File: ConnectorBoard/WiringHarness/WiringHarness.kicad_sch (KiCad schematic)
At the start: 9 parts, among them J1 Barrel_Jack, J2 Conn_01x03, J3 Conn_01x03, J4 Conn_01x04, U1 L7805, U2 L7805

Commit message: Wiring harness probably OK
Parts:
- removed J4: Conn_01x04, symbol Connector_Generic:Conn_01x04
- added C3, C4: 1uF, Capacitor_SMD:C_0603_1608Metric, symbol Device:C_Small
- added H1, H2, H3, H4: MountingHole, MountingHole:MountingHole_2.2mm_M2, symbol Mechanical:MountingHole
- added J4: Conn_02x05_Odd_Even, Connector_PinHeader_2.54mm:PinHeader_2x05_P2.54mm_Vertical, symbol Connector_Generic:Conn_02x05_Odd_Even
- C1, C2: footprint Capacitor_SMD:C_0805_2012Metric -> Capacitor_SMD:C_0603_1608Metric
- FB1: footprint (none) -> Inductor_SMD:L_0603_1608Metric
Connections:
- net Visol: now reaches C2.1, FB1.2, U2.1 (IN)
- net GND: now reaches C1.2, C2.2, J1.2, J2.3 (Pin_3), J3.3 (Pin_3), U1.2 (GND), U2.2 (GND)
- net GND: now also C3.2, C4.2, J4.2 (Pin_2)
- net Vsys: now reaches U2.3 (OUT)
- net Vsys: now also C3.1, J4.4 (Pin_4)
- net ServoY: now reaches J2.1 (Pin_1)
- net ServoY: now also J4.8 (Pin_8)
- net VoutServo: now reaches J2.2 (Pin_2), J3.2 (Pin_2), U1.3 (OUT)
- net VoutServo: now also C4.1
- net ServoX: now reaches J3.1 (Pin_1)
- net ServoX: now also J4.6 (Pin_6)
- net +12V: now reaches C1.1, FB1.1, J1.1, U1.1 (IN)
- no-connect marks 0 -> 6
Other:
- moved on the sheet: J2, J3

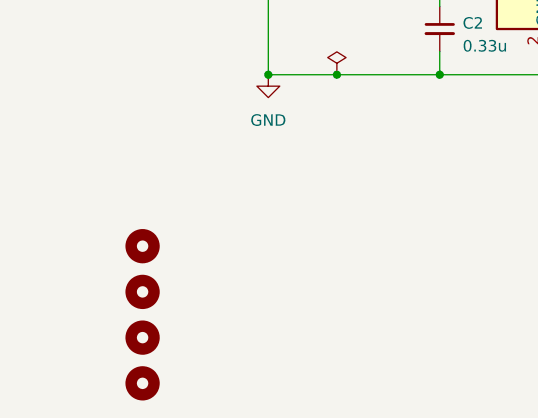
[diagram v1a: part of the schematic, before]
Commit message: Add right angle ribbon cable to wiring harness
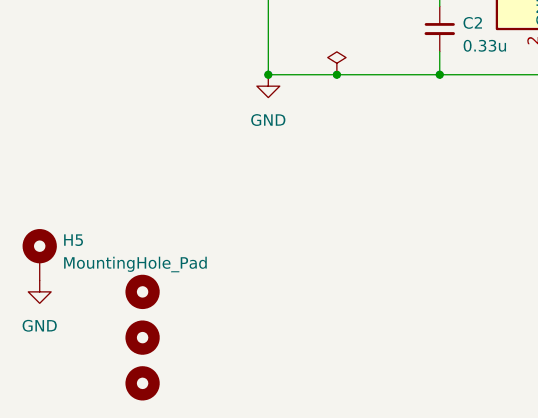
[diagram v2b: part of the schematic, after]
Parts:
- removed H1: MountingHole, MountingHole:MountingHole_2.2mm_M2, symbol Mechanical:MountingHole
- added H5: MountingHole_Pad, MountingHole:MountingHole_2.2mm_M2_Pad, symbol Mechanical:MountingHole_Pad
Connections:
- net GND: now also H5.1
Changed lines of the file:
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@@
     (effects (font (size 1.27 1.27)) (justify left bottom))
-  )
-  (symbol (lib_id "Mechanical:MountingHole") (at 60.96 109.22 0) (unit 1)
-    (in_bom yes) (on_board yes) (dnp no) (fields_autoplaced)
-    (property "Reference" "H1" (at 63.5 108.585 0)
-      (effects (font (size 1.27 1.27)) (justify left) hide)
-    )
-    (property "Value" "MountingHole" (at 63.5 111.125 0)
-      (effects (font (size 1.27 1.27)) (justify left) hide)
-    )
-    (property "Footprint" "MountingHole:MountingHole_2.2mm_M2" (at 60.96 109.22 0)
-      (effects (font (size 1.27 1.27)) hide)
-    )
-    (property "Datasheet" "~" (at 60.96 109.22 0)
-      (effects (font (size 1.27 1.27)) hide)
-    )
-    (instances
-      (project "WiringHarness"
-        (path "/91ed2d93-a6a0-4478-9f77-137103dfe05b"
-          (reference "H1") (unit 1)
-        )
-      )
-    )
   )
   (symbol (lib_id "power:GND") (at 74.93 90.17 0) (unit 1)
@@
         )
       )
+    )
+  )
+  (symbol (lib_id "power:GND") (at 49.53 113.03 0) (unit 1)
+    (in_bom yes) (on_board yes) (dnp no) (fields_autoplaced)
+    (property "Reference" "#PWR03" (at 49.53 119.38 0)
+      (effects (font (size 1.27 1.27)) hide)
+    )
+    (property "Value" "GND" (at 49.53 118.11 0)
+      (effects (font (size 1.27 1.27)))
+    )
+    (property "Footprint" "" (at 49.53 113.03 0)
+      (effects (font (size 1.27 1.27)) hide)
+    )
+    (property "Datasheet" "" (at 49.53 113.03 0)
+      (effects (font (size 1.27 1.27)) hide)
+    )
+    (pin "1")
+    (instances
+      (project "WiringHarness"
+        (path "/91ed2d93-a6a0-4478-9f77-137103dfe05b"
+          (reference "#PWR03") (unit 1)
+        )
+      )
+    )
+  )
+  (symbol (lib_id "Mechanical:MountingHole_Pad") (at 49.53 110.49 0) (unit 1)
+    (in_bom yes) (on_board yes) (dnp no) (fields_autoplaced)
+    (property "Reference" "H5" (at 52.07 108.585 0)
+      (effects (font (size 1.27 1.27)) (justify left))
+    )
+    (property "Value" "MountingHole_Pad" (at 52.07 111.125 0)
+      (effects (font (size 1.27 1.27)) (justify left))
+    )
+    (property "Footprint" "MountingHole:MountingHole_2.2mm_M2_Pad" (at 49.53 110.49 0)
+      (effects (font (size 1.27 1.27)) hide)
+    )
+    (property "Datasheet" "~" (at 49.53 110.49 0)
+      (effects (font (size 1.27 1.27)) hide)
+    )
+    (pin "1")
+    (instances
+      (project "WiringHarness"
+        (path "/91ed2d93-a6a0-4478-9f77-137103dfe05b"
+          (reference "H5") (unit 1)
+        )
+      )

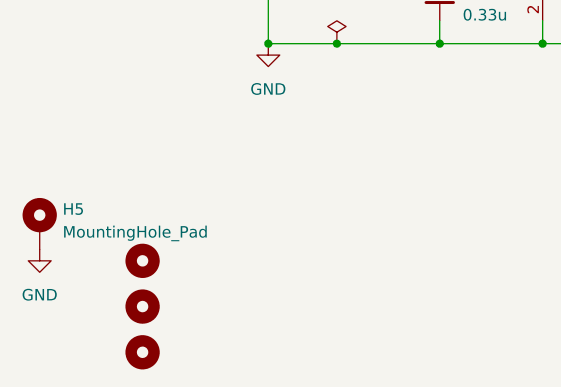
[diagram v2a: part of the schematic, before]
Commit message: Rounded corners and version string
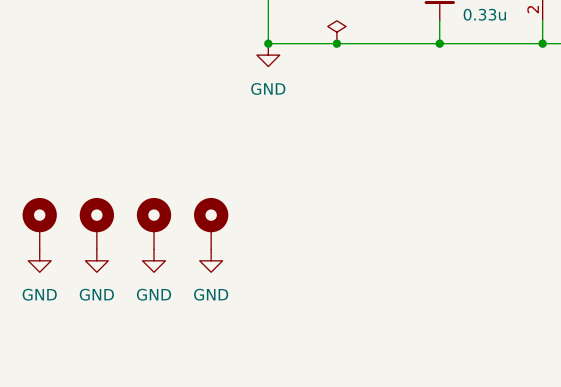
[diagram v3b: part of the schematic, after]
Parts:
- removed H2, H3, H4: MountingHole, MountingHole:MountingHole_2.2mm_M2, symbol Mechanical:MountingHole
- added H1, H2, H3: MountingHole_Pad, MountingHole:MountingHole_2.2mm_M2_Pad, symbol Mechanical:MountingHole_Pad
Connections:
- net GND: now also H1.1, H2.1, H3.1
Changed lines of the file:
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@@
     )
   )
-  (symbol (lib_id "Mechanical:MountingHole") (at 60.96 114.3 0) (unit 1)
-    (in_bom yes) (on_board yes) (dnp no) (fields_autoplaced)
-    (property "Reference" "H2" (at 63.5 113.665 0)
-      (effects (font (size 1.27 1.27)) (justify left) hide)
-    )
-    (property "Value" "MountingHole" (at 63.5 116.205 0)
-      (effects (font (size 1.27 1.27)) (justify left) hide)
-    )
-    (property "Footprint" "MountingHole:MountingHole_2.2mm_M2" (at 60.96 114.3 0)
-      (effects (font (size 1.27 1.27)) hide)
-    )
-    (property "Datasheet" "~" (at 60.96 114.3 0)
-      (effects (font (size 1.27 1.27)) hide)
-    )
-    (instances
-      (project "WiringHarness"
-        (path "/91ed2d93-a6a0-4478-9f77-137103dfe05b"
-          (reference "H2") (unit 1)
+  (symbol (lib_id "Mechanical:MountingHole_Pad") (at 55.88 110.49 0) (unit 1)
+    (in_bom yes) (on_board yes) (dnp no) (fields_autoplaced)
+    (property "Reference" "H1" (at 58.42 108.585 0)
+      (effects (font (size 1.27 1.27)) (justify left) hide)
+    )
+    (property "Value" "MountingHole_Pad" (at 58.42 111.125 0)
+      (effects (font (size 1.27 1.27)) (justify left) hide)
+    )
+    (property "Footprint" "MountingHole:MountingHole_2.2mm_M2_Pad" (at 55.88 110.49 0)
+      (effects (font (size 1.27 1.27)) hide)
+    )
+    (property "Datasheet" "~" (at 55.88 110.49 0)
+      (effects (font (size 1.27 1.27)) hide)
+    )
+    (pin "1")
+    (instances
+      (project "WiringHarness"
+        (path "/91ed2d93-a6a0-4478-9f77-137103dfe05b"
+          (reference "H1") (unit 1)
         )
       )
@@
         (path "/91ed2d93-a6a0-4478-9f77-137103dfe05b"
           (reference "#FLG02") (unit 1)
+        )
+      )
+    )
+  )
+  (symbol (lib_id "power:GND") (at 68.58 113.03 0) (unit 1)
+    (in_bom yes) (on_board yes) (dnp no) (fields_autoplaced)
+    (property "Reference" "#PWR06" (at 68.58 119.38 0)
+      (effects (font (size 1.27 1.27)) hide)
+    )
+    (property "Value" "GND" (at 68.58 118.11 0)
+      (effects (font (size 1.27 1.27)))
+    )
+    (property "Footprint" "" (at 68.58 113.03 0)
+      (effects (font (size 1.27 1.27)) hide)
+    )
+    (property "Datasheet" "" (at 68.58 113.03 0)
+      (effects (font (size 1.27 1.27)) hide)
+    )
+    (pin "1")
+    (instances
+      (project "WiringHarness"
+        (path "/91ed2d93-a6a0-4478-9f77-137103dfe05b"
+          (reference "#PWR06") (unit 1)
         )
       )
@@
     (in_bom yes) (on_board yes) (dnp no) (fields_autoplaced)
     (property "Reference" "H5" (at 52.07 108.585 0)
-      (effects (font (size 1.27 1.27)) (justify left))
+      (effects (font (size 1.27 1.27)) (justify left) hide)
     )
     (property "Value" "MountingHole_Pad" (at 52.07 111.125 0)
-      (effects (font (size 1.27 1.27)) (justify left))
+      (effects (font (size 1.27 1.27)) (justify left) hide)
     )
     (property "Footprint" "MountingHole:MountingHole_2.2mm_M2_Pad" (at 49.53 110.49 0)
@@
     )
   )
+  (symbol (lib_id "power:GND") (at 55.88 113.03 0) (unit 1)
+    (in_bom yes) (on_board yes) (dnp no) (fields_autoplaced)
+    (property "Reference" "#PWR04" (at 55.88 119.38 0)
+      (effects (font (size 1.27 1.27)) hide)
+    )
+    (property "Value" "GND" (at 55.88 118.11 0)
+      (effects (font (size 1.27 1.27)))
+    )
+    (property "Footprint" "" (at 55.88 113.03 0)
+      (effects (font (size 1.27 1.27)) hide)
+    )
+    (property "Datasheet" "" (at 55.88 113.03 0)
+      (effects (font (size 1.27 1.27)) hide)
+    )
+    (pin "1")
+    (instances
+      (project "WiringHarness"
+        (path "/91ed2d93-a6a0-4478-9f77-137103dfe05b"
+          (reference "#PWR04") (unit 1)
+        )
+      )
+    )
+  )
   (symbol (lib_id "Device:FerriteBead_Small") (at 87.63 80.01 90) (unit 1)
     (in_bom yes) (on_board yes) (dnp no) (fields_autoplaced)
@@
         (path "/91ed2d93-a6a0-4478-9f77-137103dfe05b"
           (reference "FB1") (unit 1)
+        )
+      )
+    )
+  )
+  (symbol (lib_id "Mechanical:MountingHole_Pad") (at 62.23 110.49 0) (unit 1)
+    (in_bom yes) (on_board yes) (dnp no) (fields_autoplaced)
+    (property "Reference" "H2" (at 64.77 108.585 0)
+      (effects (font (size 1.27 1.27)) (justify left) hide)
+    )
+    (property "Value" "MountingHole_Pad" (at 64.77 111.125 0)
+      (effects (font (size 1.27 1.27)) (justify left) hide)
+    )
+    (property "Footprint" "MountingHole:MountingHole_2.2mm_M2_Pad" (at 62.23 110.49 0)
+      (effects (font (size 1.27 1.27)) hide)
+    )
+    (property "Datasheet" "~" (at 62.23 110.49 0)
+      (effects (font (size 1.27 1.27)) hide)
+    )
+    (pin "1")
+    (instances
+      (project "WiringHarness"
+        (path "/91ed2d93-a6a0-4478-9f77-137103dfe05b"
+          (reference "H2") (unit 1)
+        )
+      )
+    )
+  )
+  (symbol (lib_id "Mechanical:MountingHole_Pad") (at 68.58 110.49 0) (unit 1)
+    (in_bom yes) (on_board yes) (dnp no) (fields_autoplaced)
+    (property "Reference" "H3" (at 71.12 108.585 0)
+      (effects (font (size 1.27 1.27)) (justify left) hide)
+    )
+    (property "Value" "MountingHole_Pad" (at 71.12 111.125 0)
+      (effects (font (size 1.27 1.27)) (justify left) hide)
+    )
+    (property "Footprint" "MountingHole:MountingHole_2.2mm_M2_Pad" (at 68.58 110.49 0)
+      (effects (font (size 1.27 1.27)) hide)
+    )
+    (property "Datasheet" "~" (at 68.58 110.49 0)
+      (effects (font (size 1.27 1.27)) hide)
+    )
+    (pin "1")
+    (instances
+      (project "WiringHarness"
+        (path "/91ed2d93-a6a0-4478-9f77-137103dfe05b"
+          (reference "H3") (unit 1)
         )
       )
@@
     )
   )
-  (symbol (lib_id "Mechanical:MountingHole") (at 60.96 124.46 0) (unit 1)
-    (in_bom yes) (on_board yes) (dnp no) (fields_autoplaced)
-    (property "Reference" "H4" (at 63.5 123.825 0)
-      (effects (font (size 1.27 1.27)) (justify left) hide)
-    )
-    (property "Value" "MountingHole" (at 63.5 126.365 0)
-      (effects (font (size 1.27 1.27)) (justify left) hide)
-    )
-    (property "Footprint" "MountingHole:MountingHole_2.2mm_M2" (at 60.96 124.46 0)
-      (effects (font (size 1.27 1.27)) hide)
-    )
-    (property "Datasheet" "~" (at 60.96 124.46 0)
-      (effects (font (size 1.27 1.27)) hide)
-    )
-    (instances
-      (project "WiringHarness"
-        (path "/91ed2d93-a6a0-4478-9f77-137103dfe05b"
-          (reference "H4") (unit 1)
+  (symbol (lib_id "power:GND") (at 62.23 113.03 0) (unit 1)
+    (in_bom yes) (on_board yes) (dnp no) (fields_autoplaced)
+    (property "Reference" "#PWR05" (at 62.23 119.38 0)
+      (effects (font (size 1.27 1.27)) hide)
+    )
+    (property "Value" "GND" (at 62.23 118.11 0)
+      (effects (font (size 1.27 1.27)))
+    )
+    (property "Footprint" "" (at 62.23 113.03 0)
+      (effects (font (size 1.27 1.27)) hide)
+    )
+    (property "Datasheet" "" (at 62.23 113.03 0)
+      (effects (font (size 1.27 1.27)) hide)
+    )
+    (pin "1")
+    (instances
+      (project "WiringHarness"
+        (path "/91ed2d93-a6a0-4478-9f77-137103dfe05b"
+          (reference "#PWR05") (unit 1)
         )
       )
@@
         )
       )
-    )
-  )
-  (symbol (lib_id "Mechanical:MountingHole") (at 60.96 119.38 0) (unit 1)
-    (in_bom yes) (on_board yes) (dnp no) (fields_autoplaced)
-    (property "Reference" "H3" (at 63.5 118.745 0)
-      (effects (font (size 1.27 1.27)) (justify left) hide)
-    )
-    (property "Value" "MountingHole" (at 63.5 121.285 0)
-      (effects (font (size 1.27 1.27)) (justify left) hide)
-    )
-    (property "Footprint" "MountingHole:MountingHole_2.2mm_M2" (at 60.96 119.38 0)
-      (effects (font (size 1.27 1.27)) hide)
-    )
-    (property "Datasheet" "~" (at 60.96 119.38 0)
-      (effects (font (size 1.27 1.27)) hide)
-    )
-    (instances
-      (project "WiringHarness"
-        (path "/91ed2d93-a6a0-4478-9f77-137103dfe05b"
-          (reference "H3") (unit 1)
-        )
-      )

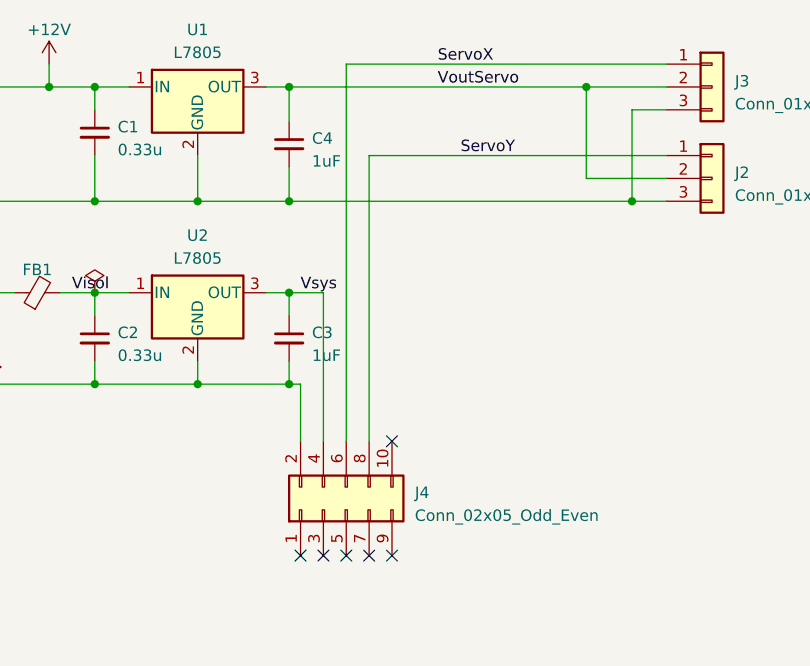
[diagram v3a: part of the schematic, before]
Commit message: Tweak the connector board a bit.  Rearrange X and Y.  May do more depending on the other board.
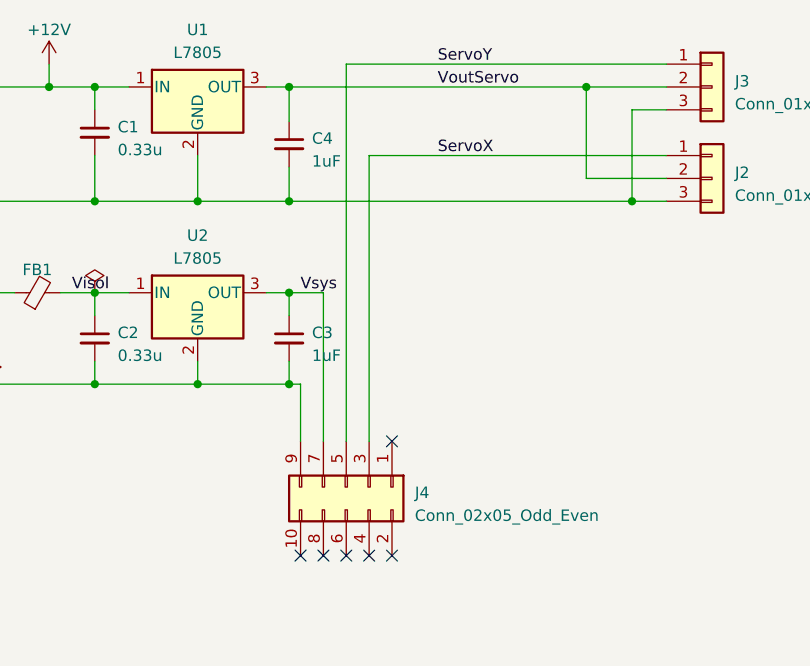
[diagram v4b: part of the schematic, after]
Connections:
- net GND: now also J4.9 (Pin_9); no longer J4.2 (Pin_2)
- net ServoX: now also J2.1 (Pin_1), J4.3 (Pin_3); no longer J3.1 (Pin_1), J4.6 (Pin_6)
- net ServoY: now also J3.1 (Pin_1), J4.5 (Pin_5); no longer J2.1 (Pin_1), J4.8 (Pin_8)
- net Vsys: now also J4.7 (Pin_7); no longer J4.4 (Pin_4)
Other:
- moved on the sheet: J4
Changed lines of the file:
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@@
     (effects (font (size 1.27 1.27)) (justify left bottom))
   )
-  (label "ServoY" (at 134.62 64.77 0) (fields_autoplaced)
+  (label "ServoX" (at 132.08 64.77 0) (fields_autoplaced)
     (effects (font (size 1.27 1.27)) (justify left bottom))
   )
@@
     (effects (font (size 1.27 1.27)) (justify left bottom))
   )
-  (label "ServoX" (at 132.08 54.61 0) (fields_autoplaced)
+  (label "ServoY" (at 132.08 54.61 0) (fields_autoplaced)
     (effects (font (size 1.27 1.27)) (justify left bottom))
   )
@@
     )
   )
-  (symbol (lib_id "Connector_Generic:Conn_02x05_Odd_Even") (at 121.92 104.14 90) (unit 1)
+  (symbol (lib_id "Connector_Generic:Conn_02x05_Odd_Even") (at 121.92 101.6 270) (unit 1)
     (in_bom yes) (on_board yes) (dnp no) (fields_autoplaced)
     (property "Reference" "J4" (at 129.54 102.235 90)
-      (effects (font (size 1.27 1.27)) (justify right))
+      (effects (font (size 1.27 1.27)) (justify left))
     )
     (property "Value" "Conn_02x05_Odd_Even" (at 129.54 104.775 90)
-      (effects (font (size 1.27 1.27)) (justify right))
-    )
-    (property "Footprint" "Connector_PinHeader_2.54mm:PinHeader_2x05_P2.54mm_Vertical" (at 121.92 104.14 0)
-      (effects (font (size 1.27 1.27)) hide)
-    )
-    (property "Datasheet" "~" (at 121.92 104.14 0)
-      (effects (font (size 1.27 1.27)) hide)
-    )
-    (property "Digikey" "732-2094-ND" (at 121.92 104.14 90)
-      (effects (font (size 1.27 1.27)) hide)
-    )
+      (effects (font (size 1.27 1.27)) (justify left))
+    )
+    (property "Footprint" "Connector_PinHeader_2.54mm:PinHeader_2x05_P2.54mm_Vertical" (at 121.92 101.6 0)
+      (effects (font (size 1.27 1.27)) hide)
+    )
+    (property "Datasheet" "~" (at 121.92 101.6 0)
+      (effects (font (size 1.27 1.27)) hide)
+    )
+    (property "Digikey" "732-2094-ND" (at 121.92 101.6 90)
+      (effects (font (size 1.27 1.27)) hide)
+    )

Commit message: updates to connector
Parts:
- removed FB1: FerriteBead_Small, Inductor_SMD:L_0603_1608Metric, symbol Device:FerriteBead_Small
- removed U2: L7805, Package_TO_SOT_SMD:TO-252-2, symbol Regulator_Linear:L7805
- added C5, C6: 1uF, Capacitor_SMD:C_0603_1608Metric, symbol Device:C_Small
- added D1: D_Schottky, Diode_SMD:D_SMA, symbol Device:D_Schottky
- added J5: Socket, Connector_PinSocket_2.54mm:PinSocket_1x04_P2.54mm_Vertical, symbol Connector_Generic:Conn_01x04
- added J6: Qwiic, Connector_JST:JST_SH_SM04B-SRSS-TB_1x04-1MP_P1.00mm_Horizontal, symbol Connector_Generic:Conn_01x04
- added JP1: SolderJumper_3_Bridged12, Jumper:SolderJumper-3_P1.3mm_Bridged12_RoundedPad1.0x1.5mm, symbol Jumper:SolderJumper_3_Bridged12
- added U2: TLV75533PDBV, Package_TO_SOT_SMD:SOT-23-5, symbol Regulator_Linear:TLV75533PDBV
- J2, J3: footprint Connector_PinHeader_1.00mm:PinHeader_1x03_P1.00mm_Horizontal -> Connector_PinHeader_2.54mm:PinHeader_1x03_P2.54mm_Horizontal
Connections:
- net Visol is gone; now on net Vsys: C2.1
- net +12V: now also D1.2 (A)
- net GND: now also C5.2, C6.2, J5.3 (Pin_3), J6.1 (Pin_1), U2.2 (GND)
- net VoutServo: now also C5.1, J5.4 (Pin_4), JP1.1 (A), U2.1 (IN), U2.3 (EN)
- net Vsys: now also D1.1 (K)
- net SCL: now reaches J4.2 (Pin_2)
- net SCL: now also J5.1 (Pin_1), J6.4 (Pin_4)
- net SDA: now reaches J4.4 (Pin_4)
- net SDA: now also J5.2 (Pin_2), J6.3 (Pin_3)
- new net: C6.1, JP1.3 (B), U2.5 (OUT)
- new net: J6.2 (Pin_2), JP1.2 (C)
- no-connect marks 6 -> 4
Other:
- note added: "Connector for 4 digit display."
- note added: "Qwiic connector is "technically" 3.3V only. We are thinking about using it to host and LSM303 which can tolerate 5V, so for now, DNP the 3.3V LDO. If we need it, it is footprinted and we can switch the jumper."
- moved on the sheet: C3

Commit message: decent candidate for rev 0.5wh
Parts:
- added J7: Header, Connector_PinHeader_2.54mm:PinHeader_1x04_P2.54mm_Horizontal, symbol Connector_Generic:Conn_01x04
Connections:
- net GND: now also J7.4 (Pin_4)
- net SCL: now also J4.3 (Pin_3); no longer J4.2 (Pin_2)
- net ServoX: now also J4.1 (Pin_1); no longer J4.3 (Pin_3)
- net ServoY: now also J4.2 (Pin_2); no longer J4.5 (Pin_5)
- net VoutServo: now also J7.3 (Pin_3)
- net Vsys: now also C1.1, U1.1 (IN)
- net D1: now reaches J4.6 (Pin_6)
- net D1: now also J7.1 (Pin_1)
- net +12V: no longer names the net of D1.2 (A), J1.1
- net +12V: no longer C1.1, U1.1 (IN)
- new net D0: J4.5 (Pin_5), J7.2 (Pin_2)
- no-connect marks 4 -> 2
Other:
- moved on the sheet: D1

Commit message: Like 0.5 candidate
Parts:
- J7: footprint Connector_PinHeader_2.54mm:PinHeader_1x04_P2.54mm_Horizontal -> Connector_JST:JST_PH_S4B-PH-K_1x04_P2.00mm_Horizontal
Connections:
- net D0: now also J7.3 (Pin_3); no longer J7.2 (Pin_2)
- net D1: now also J7.4 (Pin_4); no longer J7.1 (Pin_1)
- net GND: now also J7.1 (Pin_1); no longer J7.4 (Pin_4)
- net VoutServo: now also J7.2 (Pin_2); no longer J7.3 (Pin_3)
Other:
- moved on the sheet: J7
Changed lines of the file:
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@@
     )
   )
-  (symbol (lib_id "Connector_Generic:Conn_01x04") (at 86.36 101.6 180) (unit 1)
+  (symbol (lib_id "Connector_Generic:Conn_01x04") (at 86.36 99.06 0) (mirror y) (unit 1)
     (in_bom yes) (on_board yes) (dnp no)
     (property "Reference" "J7" (at 82.55 100.33 90)
@@
       (effects (font (size 1.27 1.27)) hide)
     )
-    (property "Footprint" "Connector_PinHeader_2.54mm:PinHeader_1x04_P2.54mm_Horizontal" (at 86.36 101.6 0)
+    (property "Footprint" "Connector_JST:JST_PH_S4B-PH-K_1x04_P2.00mm_Horizontal" (at 86.36 99.06 0)
       (effects (font (size 1.27 1.27)) hide)
     )
-    (property "Datasheet" "~" (at 86.36 101.6 0)
+    (property "Datasheet" "~" (at 86.36 99.06 0)
       (effects (font (size 1.27 1.27)) hide)
     )
